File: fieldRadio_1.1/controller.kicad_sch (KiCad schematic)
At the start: 83 parts, among them J11 Conn_01x04, J13 Conn_01x02, J14 Conn_01x02, J15 Conn_01x02, J16 Conn_01x02, J17 Conn_01x02, Q19 MOSFET-NCHANNELBSS138, U7 MIC5219-3.3YM5, Y1 32.768kHz

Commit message: Rev 1.1 layout update
layout update routing and placement
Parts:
- R100, R101, R102, R103, R104, R105, R106, R107, R108, R109, R110, R111, R112, R113, R114, R115, R116, R117, R118, R119, R120, R121, R122, R123, R124, R125, R126, R127, R128, R129, R130, R131, R132, R89, R90, R91, R92, R93, R94, R95, R96, R97, R98, R99: footprint Resistor_SMD:R_0603_1608Metric -> Resistor_SMD:R_0603_1608Metric_Pad0.98x0.95mm_HandSolder

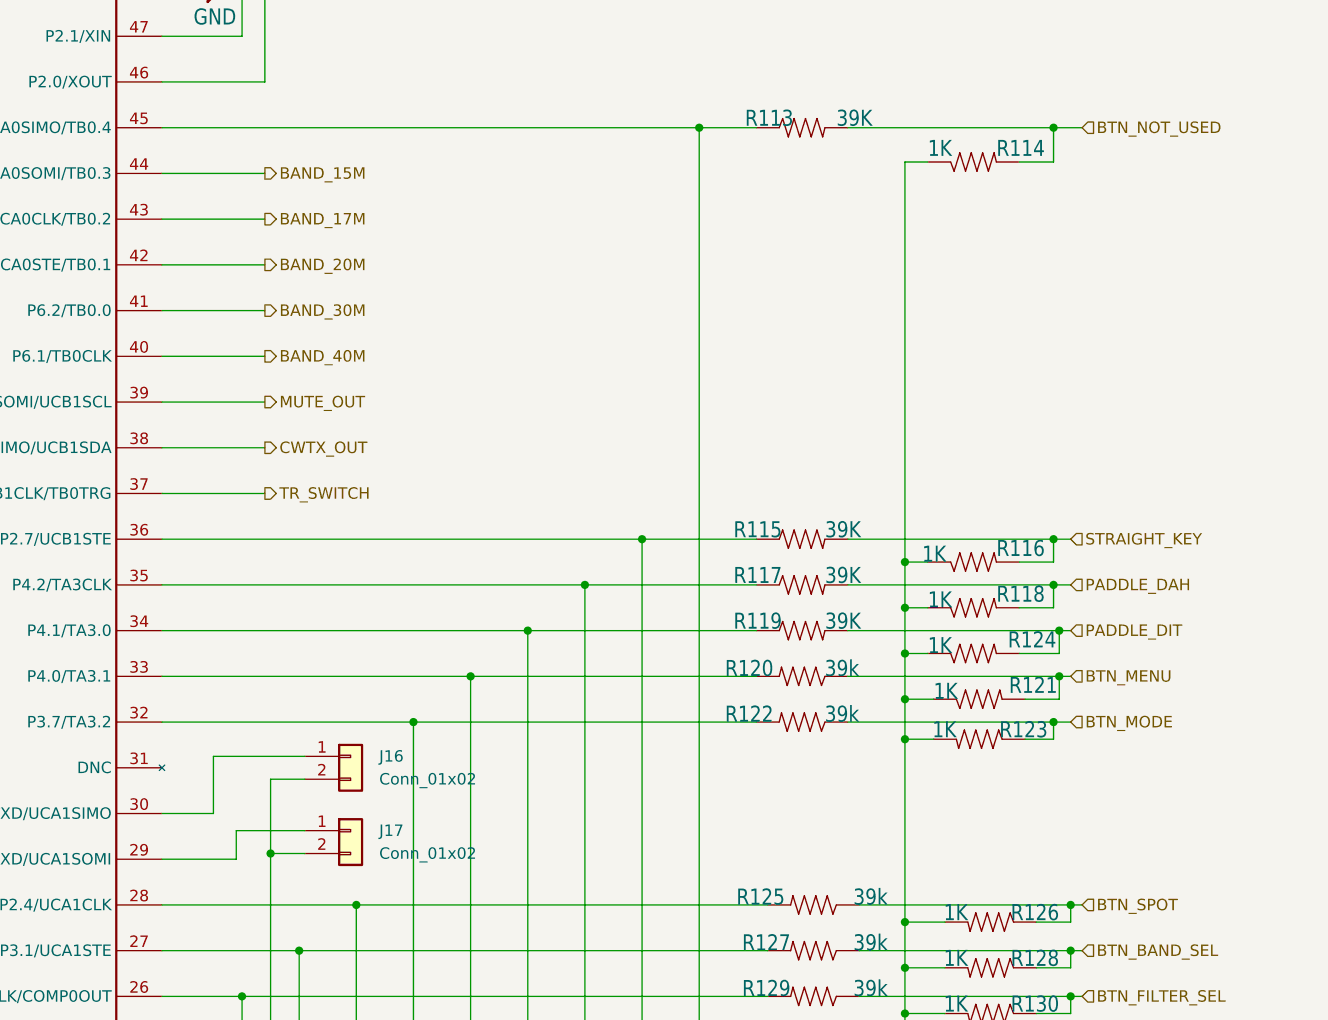
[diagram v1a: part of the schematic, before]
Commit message: Added PTT and TP for clocks
More layout cleanup and tuning.
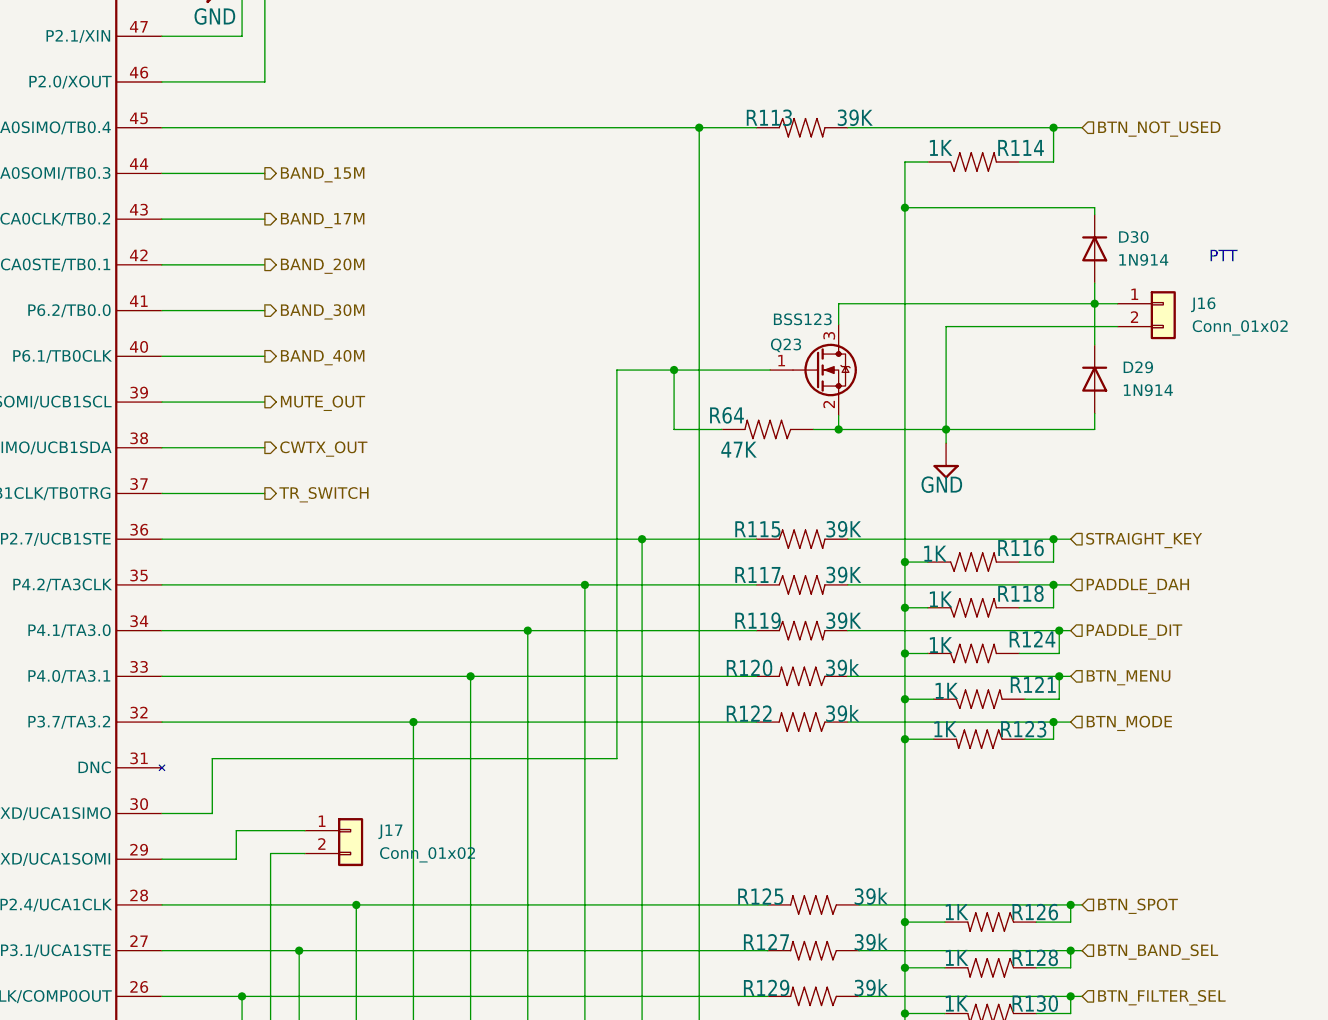
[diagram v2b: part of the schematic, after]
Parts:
- added D29, D30: 1N914, Diode_THT:D_DO-35_SOD27_P7.62mm_Horizontal, symbol Device:D
- added Q23: BSS123, Package_TO_SOT_SMD:SOT-23-3, symbol Device:Q_NMOS_GSD
- added R64: 47K, Resistor_SMD:R_0603_1608Metric_Pad0.98x0.95mm_HandSolder, symbol main-eagle-import:RESISTOR0603
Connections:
- net GND: now also D29.2 (A), Q23.2 (S), R64.1
- net VDD3.3: now also D30.1 (K)
- net at J16.1 (Pin_1): now also D29.1 (K), D30.2 (A), Q23.3 (D); no longer U$4.30 (P2.6/UCA1TXD/UCA1SIMO)
- new net: Q23.1 (G), R64.2, U$4.30 (P2.6/UCA1TXD/UCA1SIMO)
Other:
- note added: "PTT"
- moved on the sheet: J16

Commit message: Tapeout Files
button board and v1.1 radio tapeout files for JLCPCB
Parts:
- removed D29, D30: 1N914, Diode_THT:D_DO-35_SOD27_P7.62mm_Horizontal, symbol Device:D
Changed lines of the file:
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@@
   (junction (at 218.44 78.74) (diameter 0) (color 0 0 0 0)
   )
-  (junction (at 375.92 115.57) (diameter 0) (color 0 0 0 0)
-  )
   (junction (at 78.74 198.12) (diameter 0) (color 0 0 0 0)
   )
@@
   (junction (at 191.77 91.44) (diameter 0) (color 0 0 0 0)
   )
-  (junction (at 397.002 126.238) (diameter 0) (color 0 0 0 0)
-  )
   (junction (at 144.145 106.68) (diameter 0) (color 0 0 0 0)
   )
@@
     (stroke (width 0) (type default))
   )
-  (wire (pts (xy 368.554 126.238) (xy 397.002 126.238))
-    (stroke (width 0) (type default))
-  )
   (wire (pts (xy 375.92 165.1) (xy 378.46 165.1))
     (stroke (width 0) (type default))
@@
     (stroke (width 0) (type default))
   )
-  (wire (pts (xy 397.002 138.43) (xy 397.002 140.208))
-    (stroke (width 0) (type default))
-  )
   (wire (pts (xy 295.91 208.28) (xy 295.91 210.82))
     (stroke (width 0) (type default))
@@
     (stroke (width 0) (type default))
   )
-  (wire (pts (xy 375.92 110.49) (xy 375.92 115.57))
-    (stroke (width 0) (type default))
-  )
   (wire (pts (xy 390.525 194.945) (xy 394.335 194.945))
     (stroke (width 0) (type default))
@@
     (stroke (width 0) (type default))
   )
-  (wire (pts (xy 397.002 140.208) (xy 380.492 140.208))
-    (stroke (width 0) (type default))
-  )
   (wire (pts (xy 375.92 194.945) (xy 375.92 200.025))
     (stroke (width 0) (type default))
@@
     (stroke (width 0) (type default))
   )
-  (wire (pts (xy 397.002 116.332) (xy 397.002 115.57))
-    (stroke (width 0) (type default))
-  )
   (wire (pts (xy 138.43 203.2) (xy 180.34 203.2))
     (stroke (width 0) (type default))
@@
     (stroke (width 0) (type default))
   )
-  (wire (pts (xy 375.92 115.57) (xy 397.002 115.57))
-    (stroke (width 0) (type default))
-  )
   (wire (pts (xy 394.335 208.28) (xy 395.605 208.28))
     (stroke (width 0) (type default))
@@
     (stroke (width 0) (type default))
   )
-  (wire (pts (xy 397.002 123.952) (xy 397.002 126.238))
-    (stroke (width 0) (type default))
-  )
   (wire (pts (xy 186.69 218.44) (xy 186.69 220.98))
     (stroke (width 0) (type default))
@@
     (stroke (width 0) (type default))
   )
-  (wire (pts (xy 397.002 126.238) (xy 397.002 130.81))
-    (stroke (width 0) (type default))
-  )
   (wire (pts (xy 392.43 172.72) (xy 394.335 172.72))
     (stroke (width 0) (type default))
@@
     (stroke (width 0) (type default))
   )
-  (wire (pts (xy 397.002 126.238) (xy 399.542 126.238))
+  (wire (pts (xy 368.554 126.238) (xy 399.542 126.238))
     (stroke (width 0) (type default))
   )
@@
     (stroke (width 0) (type default))
   )
-  (wire (pts (xy 375.92 115.57) (xy 375.92 154.94))
+  (wire (pts (xy 375.92 110.49) (xy 375.92 154.94))
     (stroke (width 0) (type default))
   )
@@
     (stroke (width 0) (type default))
   )
-  (text "PTT" (at 409.702 121.92 0)
+  (text "PTT" (at 402.59 122.174 0)
     (effects (font (size 1.27 1.27)) (justify left bottom))
   )
@@
     )
   )
-  (symbol (lib_id "Device:D") (at 397.002 134.62 270) (unit 1)
-    (in_bom yes) (on_board yes) (dnp no) (fields_autoplaced)
-    (property "Reference" "D29" (at 400.05 133.35 90)
-      (effects (font (size 1.27 1.27)) (justify left))
-    )
-    (property "Value" "1N914" (at 400.05 135.89 90)
-      (effects (font (size 1.27 1.27)) (justify left))
-    )
-    (property "Footprint" "Diode_THT:D_DO-35_SOD27_P7.62mm_Horizontal" (at 397.002 134.62 0)
-      (effects (font (size 1.27 1.27)) hide)
-    )
-    (property "Datasheet" "~" (at 397.002 134.62 0)
-      (effects (font (size 1.27 1.27)) hide)
-    )
-    (property "Sim.Device" "D" (at 397.002 134.62 0)
-      (effects (font (size 1.27 1.27)) hide)
-    )
-    (property "Sim.Pins" "1=K 2=A" (at 397.002 134.62 0)
-      (effects (font (size 1.27 1.27)) hide)
-    )
-    (pin "1")
-    (pin "2")
-    (instances
-      (project "fieldRadio_1.1"
-        (path "/a1d1b2b0-2f27-4dc0-94ba-bb0e02933617/75918d39-3f78-4c42-b57f-e1e8147edd37"
-          (reference "D29") (unit 1)
-        )
-      )
-    )
-  )
   (symbol (lib_id "main-eagle-import:GND") (at 284.48 74.93 90) (unit 1)
     (in_bom yes) (on_board yes) (dnp no)
@@
         )
       )
-    )
-  )
-  (symbol (lib_id "Device:D") (at 397.002 120.142 270) (unit 1)
-    (in_bom yes) (on_board yes) (dnp no) (fields_autoplaced)
-    (property "Reference" "D30" (at 399.542 118.872 90)
-      (effects (font (size 1.27 1.27)) (justify left))
-    )
-    (property "Value" "1N914" (at 399.542 121.412 90)
-      (effects (font (size 1.27 1.27)) (justify left))
-    )
-    (property "Footprint" "Diode_THT:D_DO-35_SOD27_P7.62mm_Horizontal" (at 397.002 120.142 0)
-      (effects (font (size 1.27 1.27)) hide)
-    )
-    (property "Datasheet" "~" (at 397.002 120.142 0)
-      (effects (font (size 1.27 1.27)) hide)
-    )
-    (property "Sim.Device" "D" (at 397.002 120.142 0)
-      (effects (font (size 1.27 1.27)) hide)
-    )
-    (property "Sim.Pins" "1=K 2=A" (at 397.002 120.142 0)
-      (effects (font (size 1.27 1.27)) hide)
-    )
-    (pin "1")
-    (pin "2")
-    (instances
-      (project "fieldRadio_1.1"
-        (path "/a1d1b2b0-2f27-4dc0-94ba-bb0e02933617/75918d39-3f78-4c42-b57f-e1e8147edd37"
-          (reference "D30") (unit 1)
-        )
-      )
